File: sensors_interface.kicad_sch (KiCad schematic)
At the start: 14 parts, among them J5 SENSORS, Q2 DMP2240UDM-7, U4 MT3608

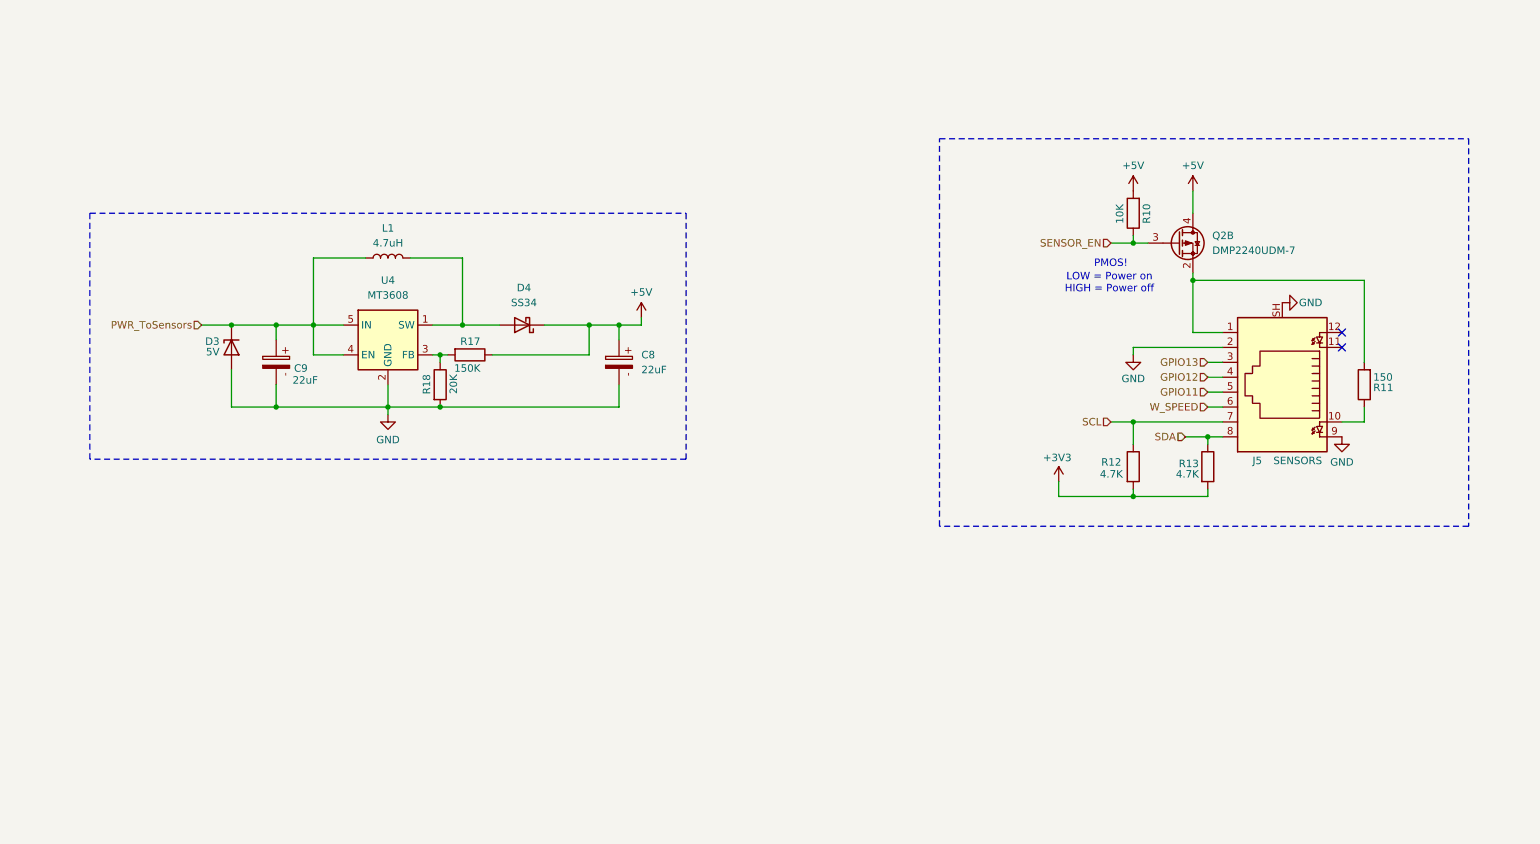
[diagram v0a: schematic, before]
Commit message: Replaced RJ45 with 1x8 P1.25mm JST connector Fix: line ends normalization for kicad files
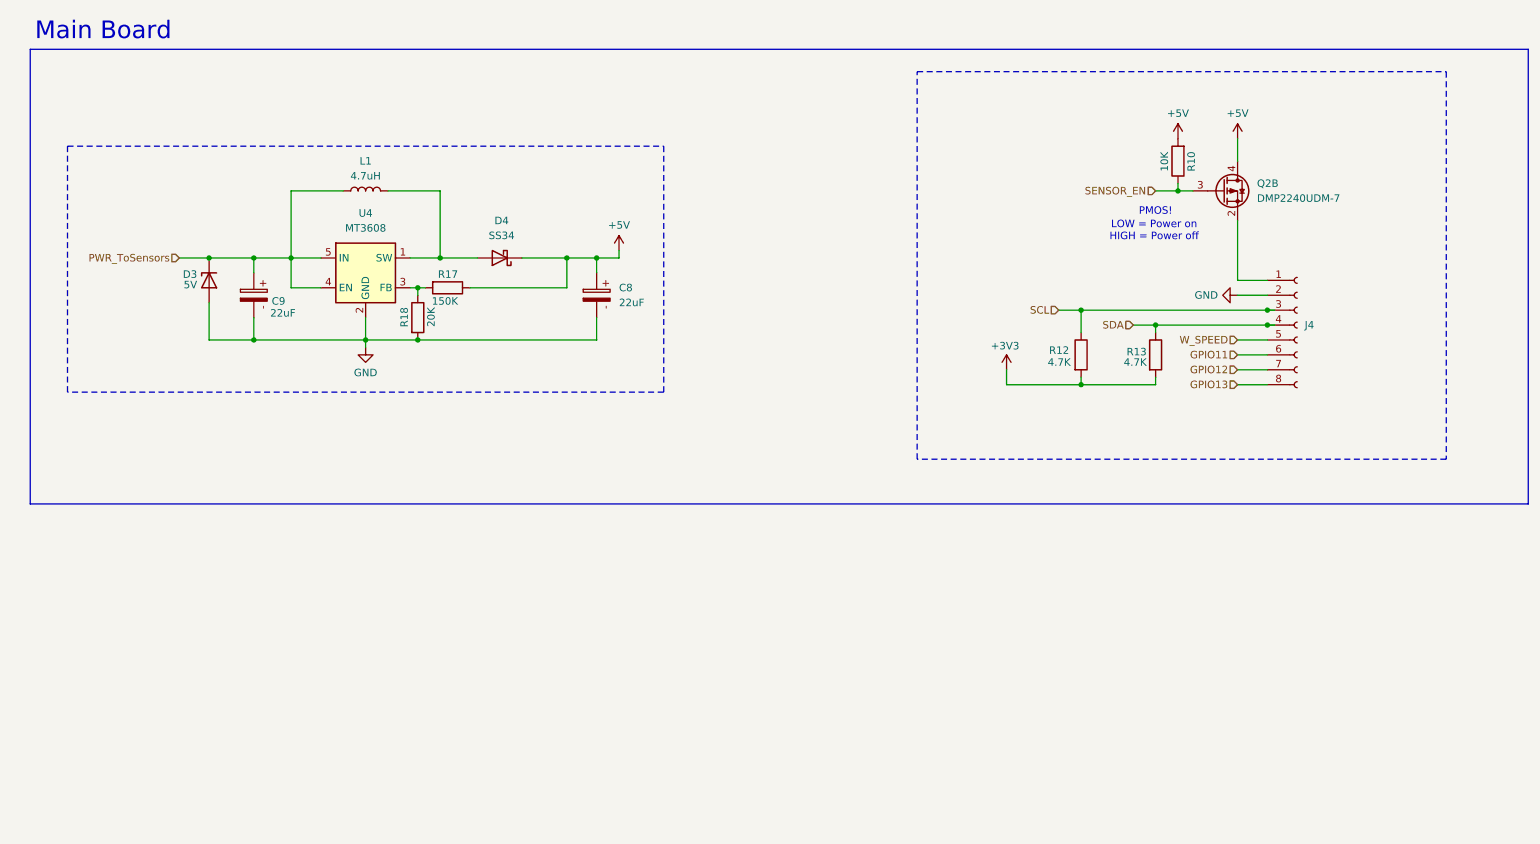
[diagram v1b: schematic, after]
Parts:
- removed J5: SENSORS, Connector_RJ:RJ45_Amphenol_RJHSE538X, symbol Connector:RJ45_LED_Shielded
- removed R11: 150, Resistor_SMD:R_1206_3216Metric, symbol Device:R
- added J4: Conn_01x08_Socket, Connector_Hirose:Hirose_DF13-08P-1.25DSA_1x08_P1.25mm_Vertical, symbol Connector:Conn_01x08_Socket
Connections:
- net GND: now also J4.2 (Pin_2)
- net GPIO11: now also J4.6 (Pin_6)
- net GPIO12: now also J4.7 (Pin_7)
- net GPIO13: now also J4.8 (Pin_8)
- net SCL: now also J4.3 (Pin_3)
- net SDA: now also J4.4 (Pin_4)
- net W_SPEED: now also J4.5 (Pin_5)
- net at Q2.2 (S): now also J4.1 (Pin_1)
- no-connect marks 2 -> 0
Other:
- note added: "Main Board"
- moved on the sheet: C8, C9, D3, D4, L1, Q2B, R10, R12, R13, R17, R18, U4

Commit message: Started the breakout board schematic
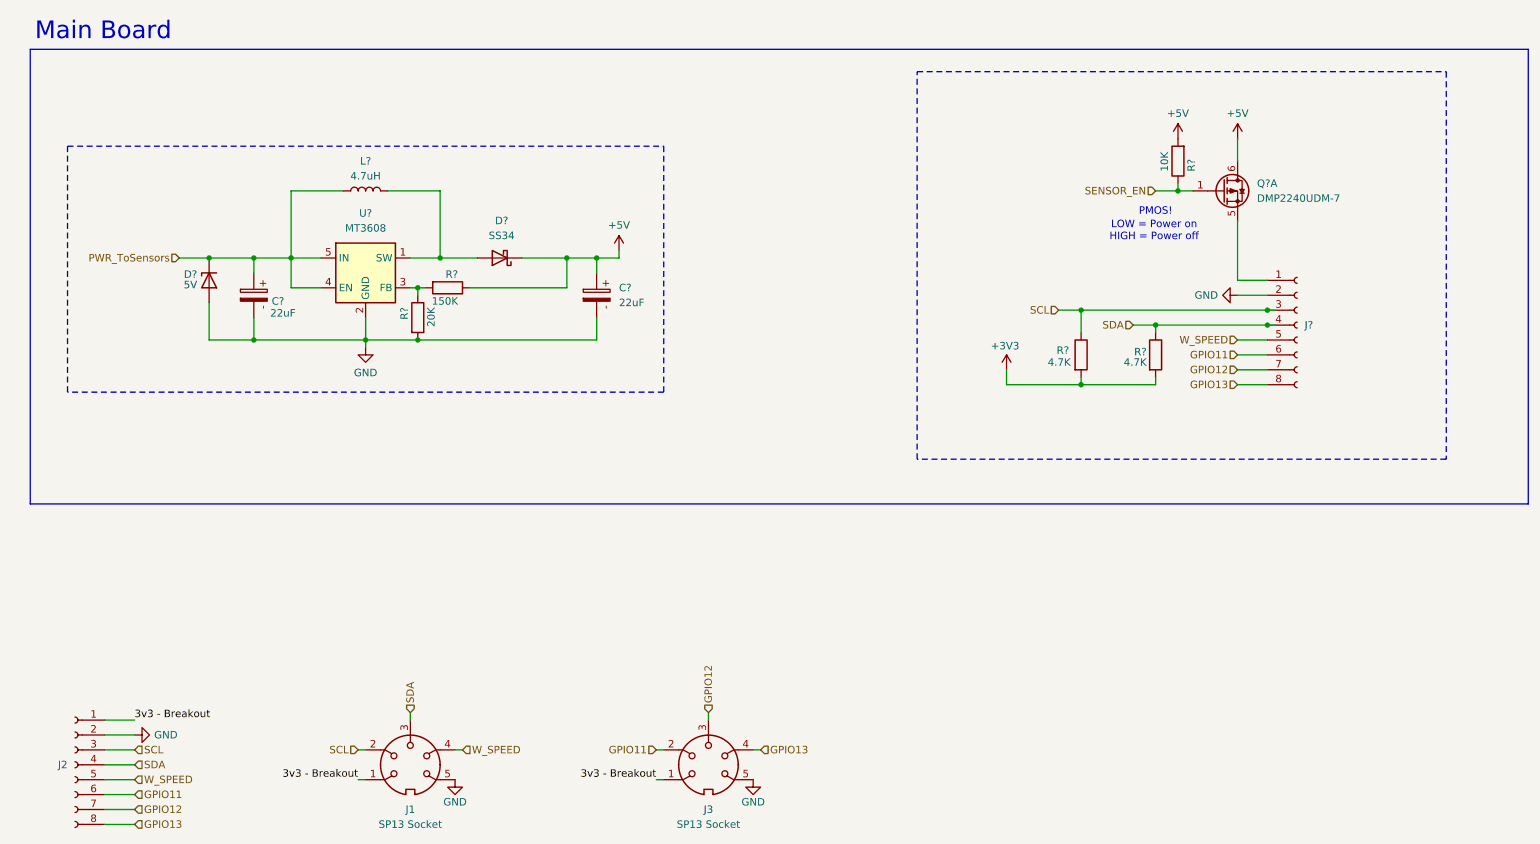
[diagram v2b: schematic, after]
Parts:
- added J1, J3: SP13 Socket, symbol Connector:DIN-5
- added J2: Conn_01x08_Socket, Connector_Hirose:Hirose_DF13-08P-1.25DSA_1x08_P1.25mm_Vertical, symbol Connector:Conn_01x08_Socket
- renumbered C9 to C?, C8 to C?, D3 to D?, D4 to D?, J4 to J?, L1 to L?, Q2 to Q?, R10 to R?, R17 to R?, R18 to R?, R12 to R?, R13 to R?, U4 to U?
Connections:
- net +5V: now also Q?.6 (D); no longer Q?.4 (D)
- net GND: now also J1.5, J2.2 (Pin_2), J3.5
- net GPIO11: now also J2.6 (Pin_6), J3.2
- net GPIO12: now also J2.7 (Pin_7), J3.3
- net GPIO13: now also J2.8 (Pin_8), J3.4
- net SCL: now also J1.2, J2.3 (Pin_3)
- net SDA: now also J1.3, J2.4 (Pin_4)
- net SENSOR_EN: now also Q?.1 (G); no longer Q?.3 (G)
- net W_SPEED: now also J1.4, J2.5 (Pin_5)
- net at J?.1 (Pin_1): now also Q?.5 (S); no longer Q?.2 (S)
- new net 3v3 - Breakout: J1.1, J2.1 (Pin_1), J3.1

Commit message: Added breakoout board - no panelization done yet Manufacturing capabilities have not been checked
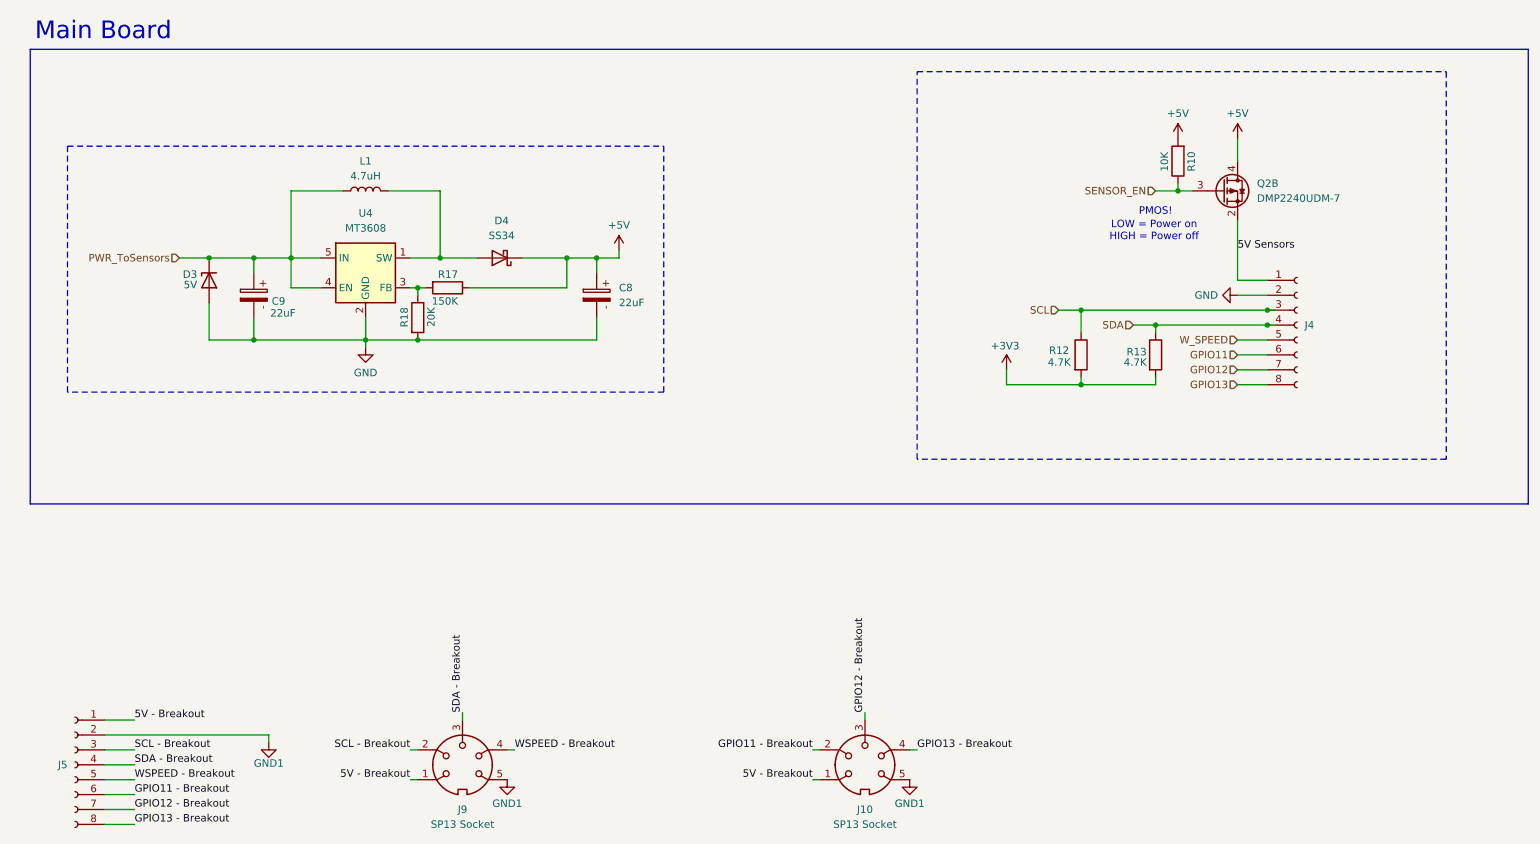
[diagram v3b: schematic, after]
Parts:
- J10: renamed from J3; footprint (none) -> SP13_5pin_holes:SP13_5pin_holes
- J9: renamed from J1; footprint (none) -> SP13_5pin_holes:SP13_5pin_holes
- gave numbers to parts that had none: 13
- renumbered J2 to J5
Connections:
- net +5V: now also Q2.4 (D); no longer Q2.6 (D)
- net GND: no longer J10.5, J5.2 (Pin_2), J9.5
- net GPIO11: no longer J10.2, J5.6 (Pin_6)
- net GPIO12: no longer J10.3, J5.7 (Pin_7)
- net GPIO13: no longer J10.4, J5.8 (Pin_8)
- net SCL: no longer J5.3 (Pin_3), J9.2
- net SDA: no longer J5.4 (Pin_4), J9.3
- net SENSOR_EN: now also Q2.3 (G); no longer Q2.1 (G)
- net W_SPEED: no longer J5.5 (Pin_5), J9.4
- net 5V Sensors: now reaches J4.1 (Pin_1)
- net 5V Sensors: now also Q2.2 (S); no longer Q2.5 (S)
- net 3v3 - Breakout renamed 5V - Breakout
- new net GND1: J10.5, J5.2 (Pin_2), J9.5
- new net GPIO11 - Breakout: J10.2, J5.6 (Pin_6)
- new net GPIO12 - Breakout: J10.3, J5.7 (Pin_7)
- new net GPIO13 - Breakout: J10.4, J5.8 (Pin_8)
- new net SCL - Breakout: J5.3 (Pin_3), J9.2
- new net SDA - Breakout: J5.4 (Pin_4), J9.3
- new net WSPEED - Breakout: J5.5 (Pin_5), J9.4
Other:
- moved on the sheet: J10, J9

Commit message: Now sensor power gets switched before 5V boost-coverter Reduced 3.3v plane size
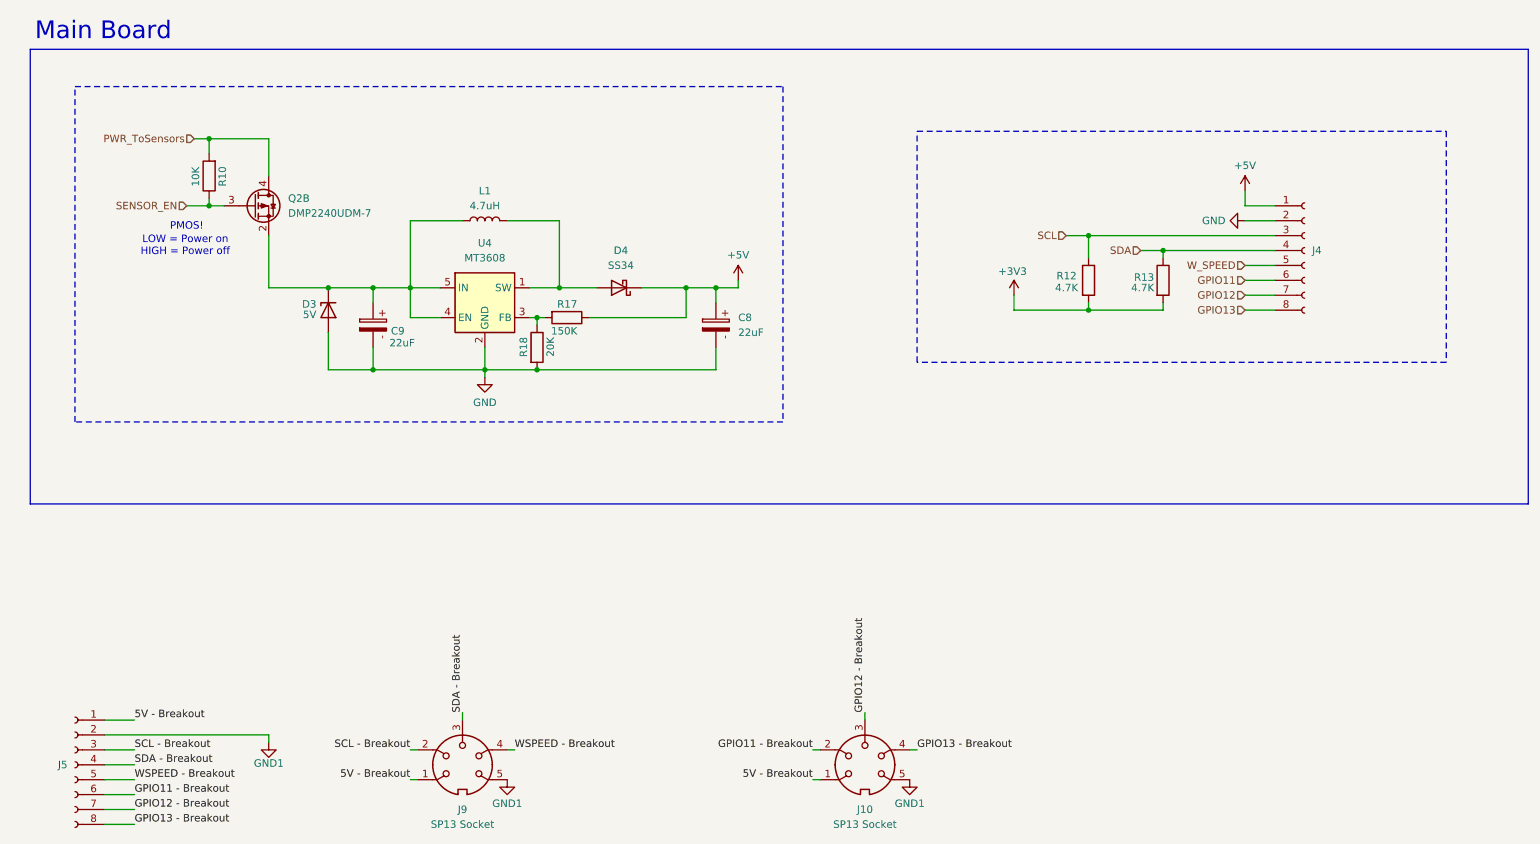
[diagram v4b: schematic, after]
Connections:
- net +5V: now also J4.1 (Pin_1); no longer Q2.4 (D), R10.2
- net PWR_ToSensors: now also Q2.4 (D), R10.2; no longer C9.1, D3.1 (K), L1.1, U4.4 (EN), U4.5 (IN)
- net 5V Sensors: no longer names the net of Q2.2 (S)
- net 5V Sensors: now also C9.1, D3.1 (K), L1.1, U4.4 (EN), U4.5 (IN); no longer J4.1 (Pin_1)
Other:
- moved on the sheet: C8, C9, D3, D4, J4, L1, R10, R12, R13, R17, R18, U4

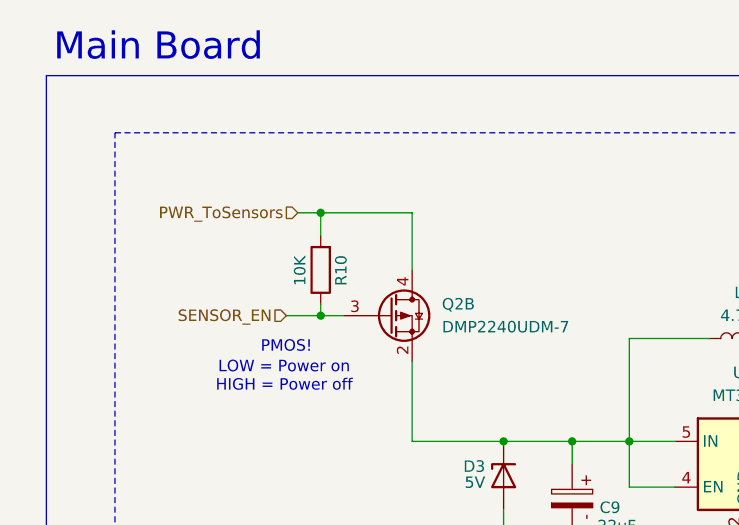
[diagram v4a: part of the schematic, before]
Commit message: - Changed CHRG and STDBY pins to 48 and 47 (CHRG was strapping) - Exposed 5V rail do Breakout connector. Now also it matches a bme280 pinout for testing - Renamed BatteryReg net to Battery_SW - Fixed connection to 5V converter - Changed to USBLC6-2SC6 for ESD Protection - Fixed mirrored VEML7700 footprint
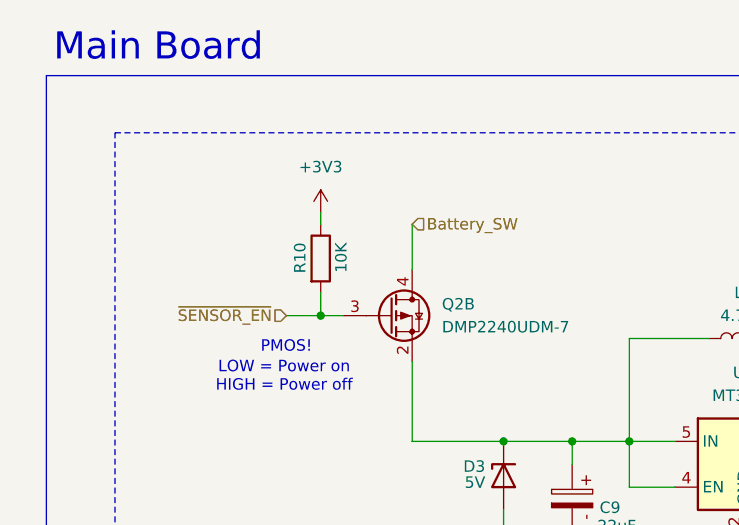
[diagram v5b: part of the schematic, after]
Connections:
- net +3V3: now also R10.1
- net PWR_ToSensors renamed Battery_SW
- net Battery_SW: no longer R10.2
- net SENSOR_EN renamed ~{SENSOR_EN}
- net ~{SENSOR_EN}: now also R10.2; no longer R10.1
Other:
- moved on the sheet: R10
